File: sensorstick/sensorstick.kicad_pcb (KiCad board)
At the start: 4 copper layers, 39.2 x 28.4 mm, 20 parts, among them J1 U217-04XN-XXR84, U1 ESP32-C3_SUPERMINI, U2 SGP30, U3 SHT4x, U4 SCD40-D-R2, U5 TPS71533__SC70, U6 2N7002DW

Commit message: added jcsc part numbers
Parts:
- C6: value 0μF -> 470nF
- J1: value U217-04XN-XXR84 -> USB-A Header
- RN1, RN2: value 2D02WGJ0103TCE -> 2x 100k Array
- RN3: value 4D02WGF1002TCE -> 4x 100k Array
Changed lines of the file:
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@@
 			)
 		)
-		(property "Value" "U217-04XN-XXR84"
+		(property "Value" "USB-A Header"
 			(at 0 7.95 270)
 			(layer "F.Fab")
@@
 			)
 		)
-		(property "Value" "0μF"
+		(property "Value" "470nF"
 			(at 0 -1.43 0)
 			(layer "B.Fab")
@@
 			)
 		)
-		(property "Datasheet" ""
+		(property "Datasheet" "https://www.lcsc.com/datasheet/C1623.pdf"
 			(at 0 0 180)
 			(unlocked yes)
@@
 			)
 		)
+		(property "LCSC" "C1623"
+			(at 0 0 0)
+			(layer "B.SilkS")
+			(hide yes)
+			(effects
+				(font
+					(size 1.27 1.27)
+					(thickness 0.15)
+				)
+			)
+		)
 		(property ki_fp_filters "C_*")
 		(sheetname "/")
@@
 			)
 		)
+		(property "LCSC" "C407576"
+			(at 0 0 0)
+			(layer "B.SilkS")
+			(hide yes)
+			(effects
+				(font
+					(size 1.27 1.27)
+					(thickness 0.15)
+				)
+			)
+		)
 		(property ki_fp_filters "R_*")
 		(sheetname "/")
@@
 			)
 		)
-		(property "Value" "2D02WGJ0103TCE"
+		(property "Value" "2x 100k Array"
 			(at 0 -4.32 0)
 			(layer "B.Fab")
@@
 			)
 		)
+		(property "LCSC" "C2765527"
+			(at 0 0 0)
+			(unlocked yes)
+			(layer "B.Fab")
+			(hide yes)
+			(effects
+				(font
+					(size 1 1)
+					(thickness 0.15)
+				)
+				(justify mirror)
+			)
+		)
 		(sheetname "/")
 		(sheetfile "sensorstick.kicad_sch")
@@
 			)
 		)
-		(property "Datasheet" ""
+		(property "Datasheet" "https://www.lcsc.com/datasheet/C232839.pdf"
 			(at 0 0 90)
 			(layer "B.Fab")
@@
 			)
 		)
+		(property "LCSC" "C1591"
+			(at 0 0 0)
+			(layer "B.SilkS")
+			(hide yes)
+			(effects
+				(font
+					(size 1.27 1.27)
+					(thickness 0.15)
+				)
+			)
+		)
 		(property ki_fp_filters "C_*")
 		(sheetname "/")
@@
 			)
 		)
-		(property "Value" "4D02WGF1002TCE"
+		(property "Value" "4x 100k Array"
 			(at 0 -4.43 90)
 			(layer "B.Fab")
@@
 			)
 		)
+		(property "LCSC" "C414600"
+			(at 0 0 270)
+			(unlocked yes)
+			(layer "B.Fab")
+			(hide yes)
+			(effects
+				(font
+					(size 1 1)
+					(thickness 0.15)
+				)
+				(justify mirror)
+			)
+		)
 		(sheetname "/")
 		(sheetfile "sensorstick.kicad_sch")
@@
 			)
 		)
+		(property "LCSC" "C9900163442"
+			(at 0 0 0)
+			(layer "B.SilkS")
+			(hide yes)
+			(effects
+				(font
+					(size 1.27 1.27)
+					(thickness 0.15)
+				)
+			)
+		)
 		(property ki_fp_filters "R_*")
 		(sheetname "/")
@@
 			)
 		)
-		(property "Value" "2D02WGJ0103TCE"
+		(property "Value" "2x 100k Array"
 			(at 0 -4.32 90)
 			(layer "B.Fab")
@@
 			)
 		)
+		(property "LCSC" "C2765527"
+			(at 0 0 270)
+			(unlocked yes)
+			(layer "B.Fab")
+			(hide yes)
+			(effects
+				(font
+					(size 1 1)
+					(thickness 0.15)
+				)
+				(justify mirror)
+			)
+		)
 		(sheetname "/")
 		(sheetfile "sensorstick.kicad_sch")
@@
 			)
 		)
+		(property "LCSC" "C182013"
+			(at 0 0 180)
+			(unlocked yes)
+			(layer "B.Fab")
+			(hide yes)
+			(effects
+				(font
+					(size 1 1)
+					(thickness 0.15)
+				)
+				(justify mirror)
+			)
+		)
 		(sheetname "/")
 		(sheetfile "sensorstick.kicad_sch")
@@
 			)
 		)
-		(property "LCSC" "C14663"
+		(property "LCSC" "C1591"
 			(at 0 0 90)
 			(unlocked yes)
@@
 			)
 		)
-		(property "LCSC" "C14663"
+		(property "LCSC" "C1591"
 			(at 0 0 180)
 			(unlocked yes)
@@
 			)
 		)
+		(property "LCSC" "C571193"
+			(at 0 0 0)
+			(layer "B.SilkS")
+			(hide yes)
+			(effects
+				(font
+					(size 1.27 1.27)
+					(thickness 0.15)
+				)
+			)
+		)

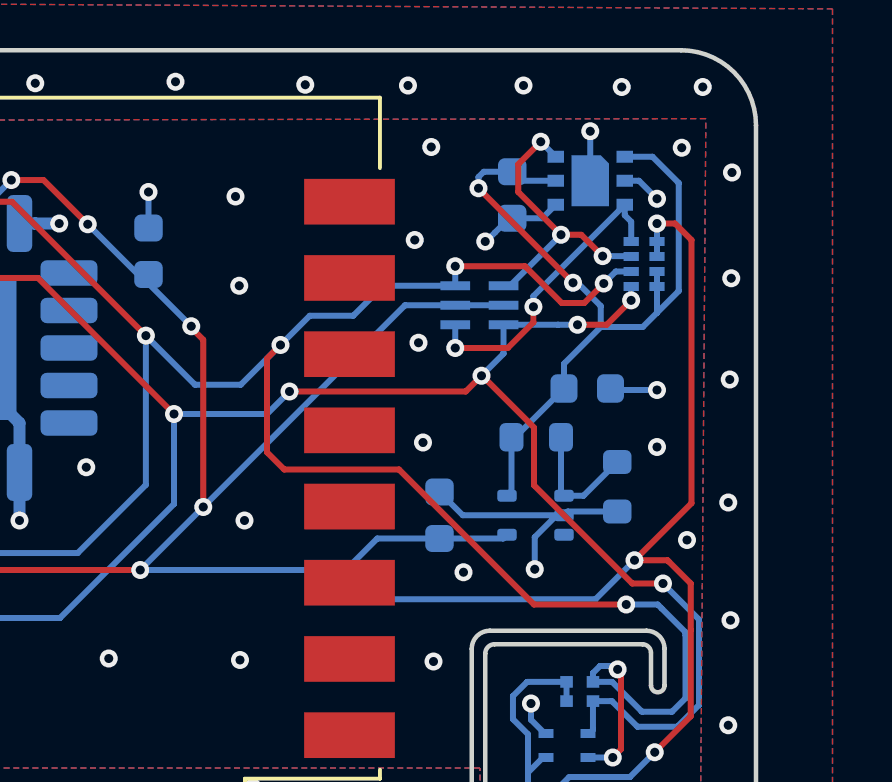
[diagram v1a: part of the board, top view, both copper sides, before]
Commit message: changed 3,3 to 1,8 module and i2c level shifter
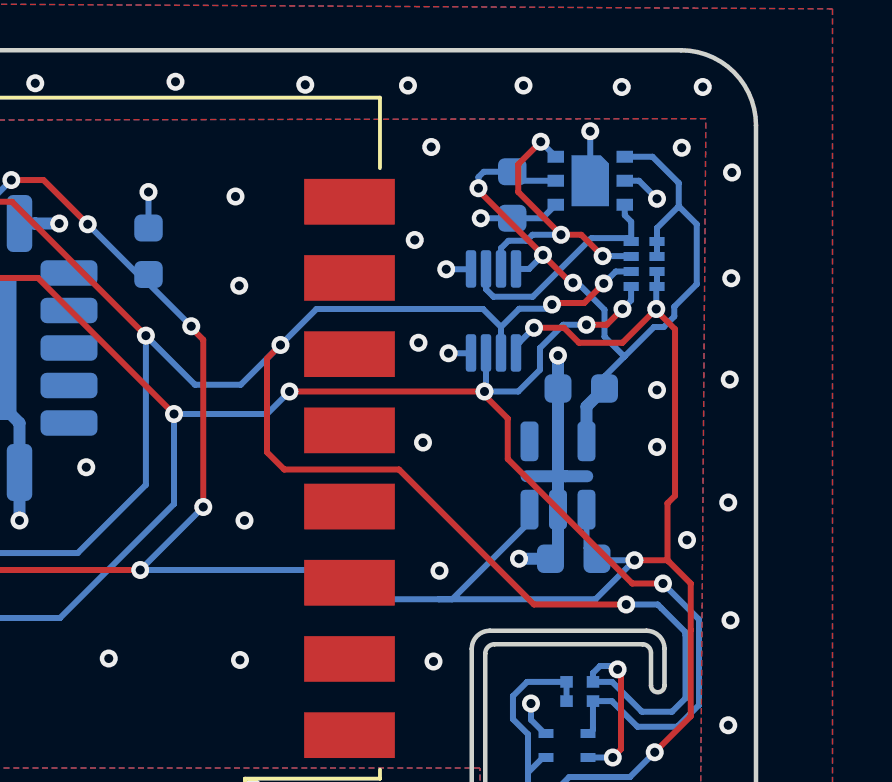
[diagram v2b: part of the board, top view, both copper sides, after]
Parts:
- removed C6: 470nF, Capacitor_SMD:C_0603_1608Metric
- removed R7: 499kΩ, Resistor_SMD:R_0603_1608Metric
- removed R8: 1MΩ, Resistor_SMD:R_0603_1608Metric
- removed U5: TPS71533__SC70, Package_TO_SOT_SMD:SOT-353_SC-70-5
- added C8: 1µF, Capacitor_SMD:C_0603_1608Metric, B.Cu at (92.7, 96.9)
- added U7: SN74LVC2T45DCUR, Package_SO:VSSOP-8_2.3x2mm_P0.5mm, B.Cu at (89.8, 94.3)
- C7: value 100nF -> 1µF
- U4: value SCD40-D-R2 -> SCD40
- U6: value 2N7002DW -> LP5907MFX-1.8; footprint 2N7002DW:SOT363 -> Package_TO_SOT_SMD:SOT-23-5
- moved U6 6.25 mm to (91.9, 99.8)
- moved C7 4.70 mm to (92.4, 102.6), turned to 180 degrees
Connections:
- RN3 pad 5: +1.8V -> +3.3V
- RN3 pad 6: +1.8V -> +3.3V
- RN3 pad 7: +3.3V -> +1.8V
- RN3 pad 8: +3.3V -> +1.8V
- U6 pad 1: /IC2_SDA_1.8 -> +3.3V
- U6 pad 2: +3.3V -> GND
- U6 pad 3: /I2C_SCL_3.3 -> +3.3V
- U6 pad 4: /I2C_SCL_1.8 -> unconnected-(U6-NC-Pad4)
- U6 pad 5: +3.3V -> +1.8V
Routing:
- net +3.3V: track 104.4 -> 95.1 mm, vias 10 -> 11
- net Net-(U5-FB): track 4.23 -> 0.00 mm
- net /IC2_SDA_1.8: track 10.3 -> 7.79 mm, vias 2 -> 0
- net GND: track 47.5 -> 49.0 mm, vias 35 -> 38
- net /IC2_SDA_3.3: track 70.0 -> 70.7 mm
- net +1.8V: track 26.3 -> 26.2 mm, vias 2 -> 3

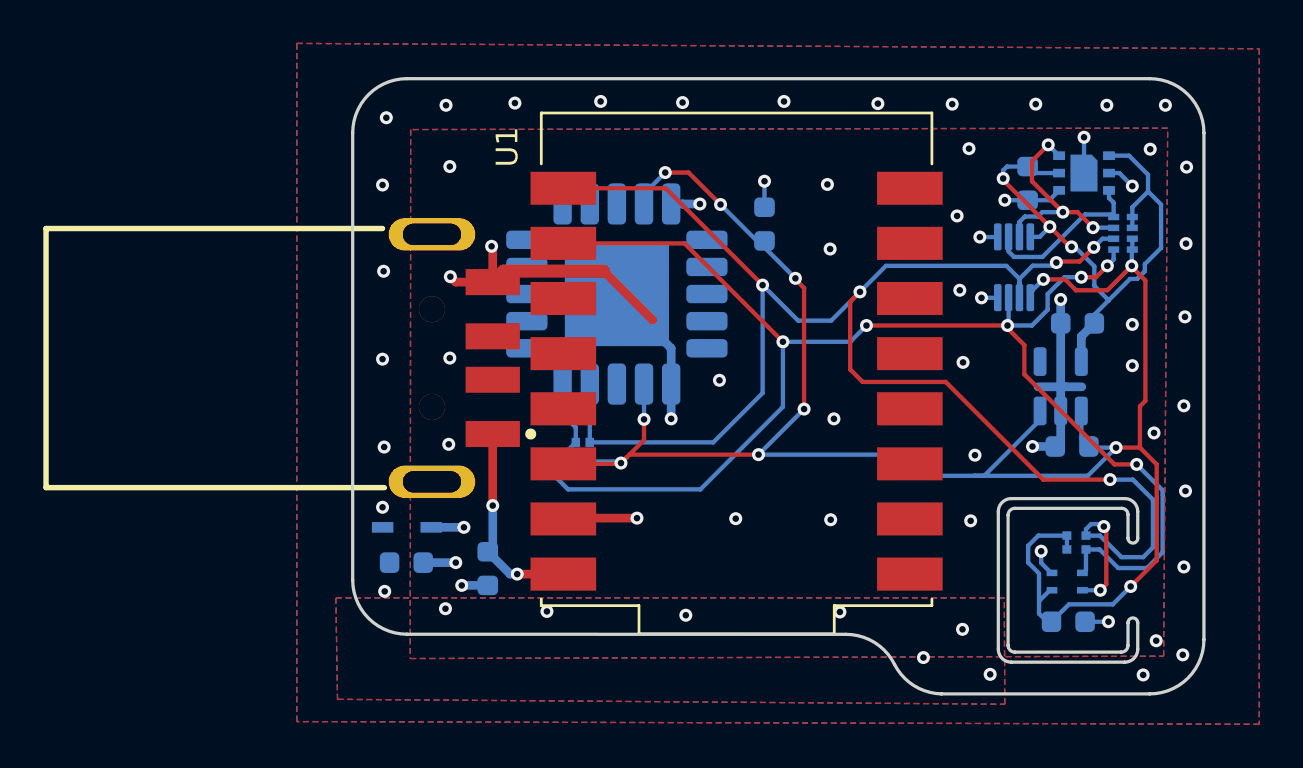
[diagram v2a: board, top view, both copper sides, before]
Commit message: changed rev number to 2
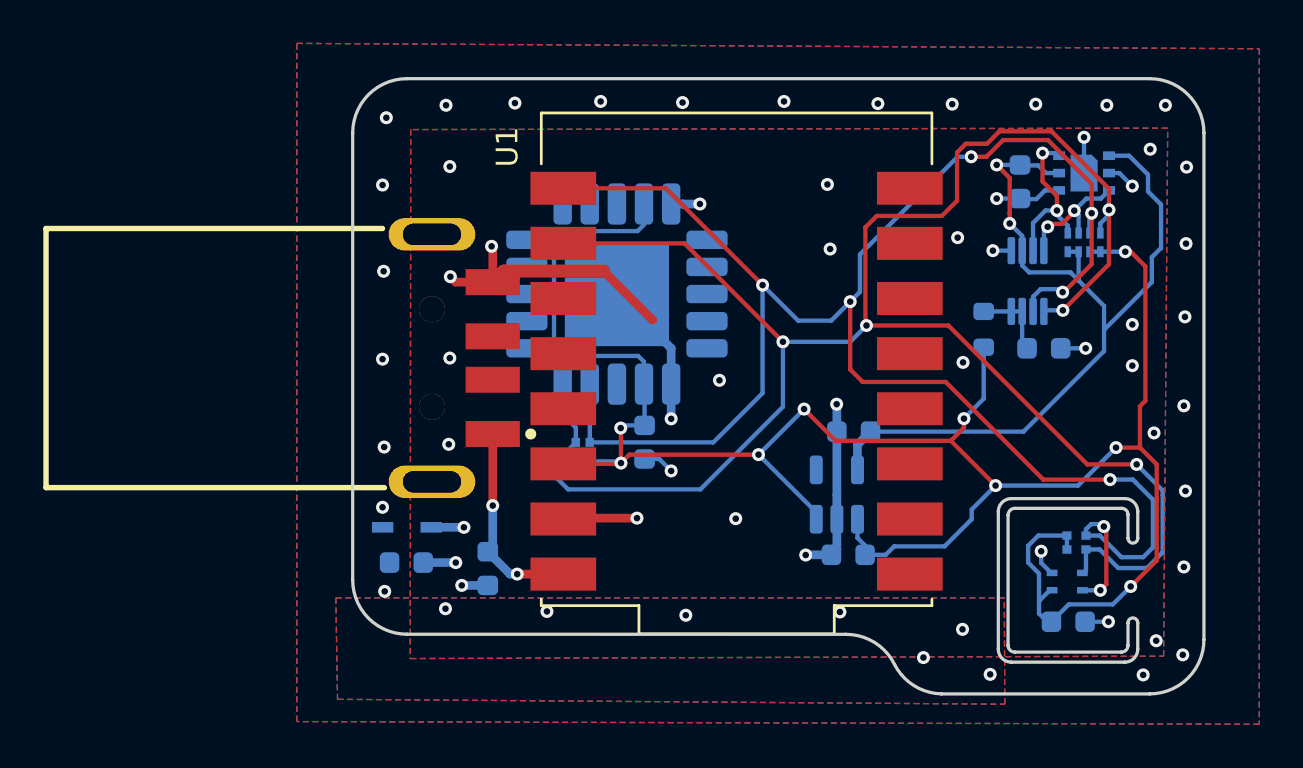
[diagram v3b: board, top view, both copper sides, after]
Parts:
- removed U7: SN74LVC2T45DCUR, Package_SO:VSSOP-8_2.3x2mm_P0.5mm
- added C6: 100nF, Capacitor_SMD:C_0603_1608Metric, B.Cu at (91.1, 98.0)
- added R1: 200 kΩ, Resistor_SMD:R_0603_1608Metric, B.Cu at (88.3, 97.2)
- added U5: PCA9306DC, Package_SO:VSSOP-8_2.3x2mm_P0.5mm, B.Cu at (90.4, 95.0)
- U4: value SCD40 -> SCD40-D-R2
- moved C1 11.5 mm to (72.7, 102.4), turned to 90 degrees
- moved U6 11.5 mm to (81.6, 104.8)
- moved C7 11.5 mm to (82.1, 107.6)
- moved C8 11.5 mm to (82.4, 101.9)
- moved RN3 1.84 mm to (93.0, 93.2), turned to 180 degrees
- moved C2 0.36 mm to (90.0, 90.4)
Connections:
- RN3 pad 1: /IC2_SDA_1.8 -> /IC2_SDA_3.3
- RN3 pad 2: /I2C_SCL_1.8 -> /I2C_SCL_3.3
- RN3 pad 3: /I2C_SCL_3.3 -> /IC2_SDA_1.8
- RN3 pad 4: /IC2_SDA_3.3 -> /I2C_SCL_1.8
- RN3 pad 5: +3.3V -> +1.8V
- RN3 pad 6: +3.3V -> +1.8V
- RN3 pad 7: +1.8V -> +3.3V
- RN3 pad 8: +1.8V -> +3.3V
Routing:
- net /IC2_SDA_3.3: track 70.7 -> 90.0 mm, vias 6 -> 5
- net +1.8V: track 26.2 -> 41.6 mm, vias 3 -> 2
- net /I2C_SCL_3.3: track 78.8 -> 88.1 mm, vias 7 -> 8
- net +3.3V: track 95.1 -> 102.2 mm, vias 11 -> 9
- net Net-(U5-EN): track 0.00 -> 3.57 mm
- net /I2C_SCL_1.8: track 10.3 -> 7.59 mm, vias 3 -> 2
- net /IC2_SDA_1.8: track 7.79 -> 5.88 mm, vias 0 -> 2
- net GND: track 49.0 -> 48.0 mm, vias 38 -> 32
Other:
- board text added: "${TITLE} by ${COMPANY} (rev. 2) ${COMMENT1}"
- board text removed: "${TITLE} by ${COMPANY} (rev. ${REVISION}) ${COMMENT1}"

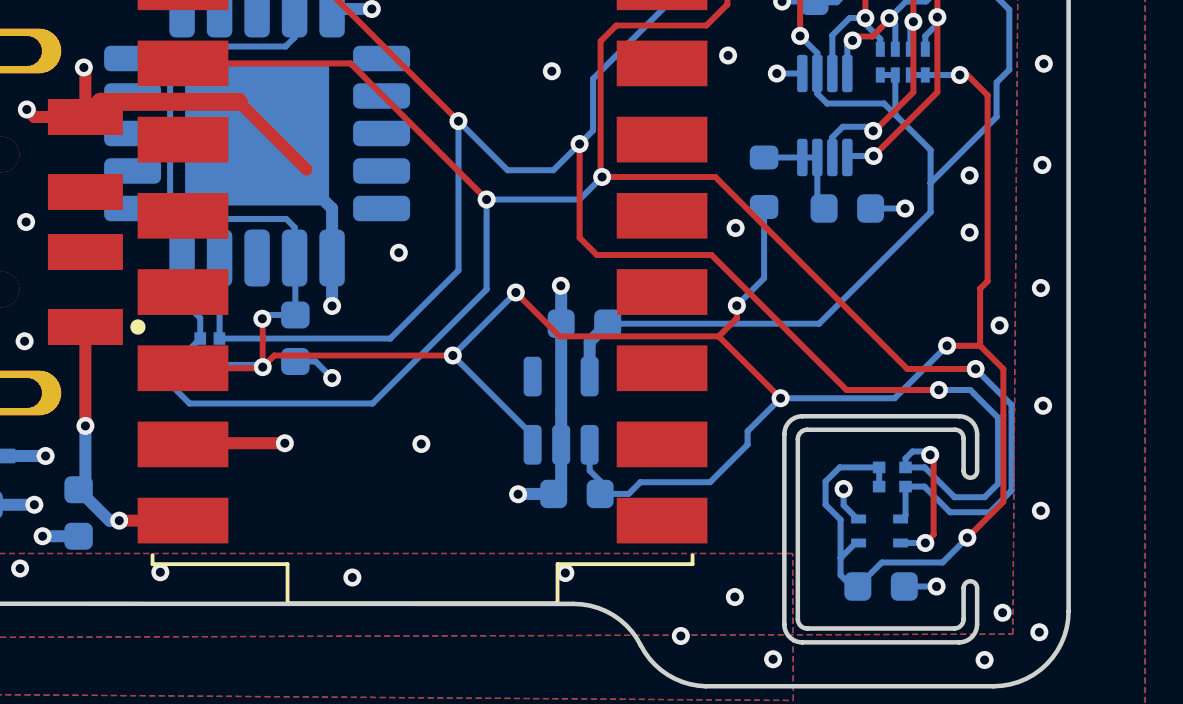
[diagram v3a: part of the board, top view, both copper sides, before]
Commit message: added NTC for board Temperature and finaly touch bevore ordering the PCB
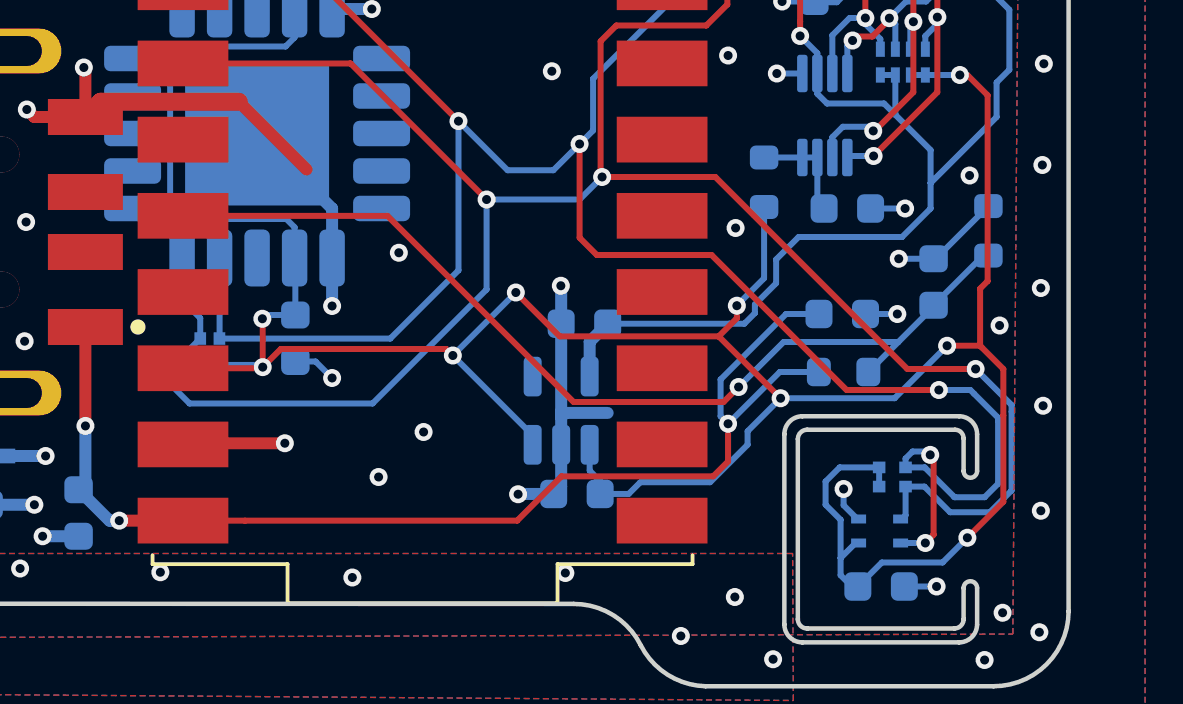
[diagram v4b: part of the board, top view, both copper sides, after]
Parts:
- added C10: 10µF, Capacitor_SMD:C_0603_1608Metric, B.Cu at (91.0, 101.6)
- added C9: 0.1µF, Capacitor_SMD:C_0603_1608Metric, B.Cu at (94.0, 100.5)
- added R2: 10 kΩ, Resistor_SMD:R_0603_1608Metric, B.Cu at (95.8, 98.8)
- added TH1: 10 kΩ NTC, Resistor_SMD:R_0603_1608Metric, B.Cu at (91.0, 103.5)
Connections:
- U1 pad 3: unconnected-(U1-GPIO3-Pad3) -> /ADC_1_3
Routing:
- net /ADC_1_3: track 0.00 -> 32.9 mm, vias 0 -> 1
- net +5V: track 9.75 -> 39.5 mm, vias 2 -> 3
- net GND: track 48.0 -> 54.5 mm, vias 32 -> 34
- net +1.8V: track 41.6 -> 42.1 mm
